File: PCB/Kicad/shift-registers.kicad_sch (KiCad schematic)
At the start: 7 parts

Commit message: routing
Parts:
- renumbered UVU-LINE3 to UVU-LINE1, UVU-LINE1 to UVU-LINE3
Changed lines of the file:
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@@
-(kicad_sch (version 20210126) (generator eeschema)
+(kicad_sch (version 20210406) (generator eeschema)
   (paper "A4")
   (no_connect (at 109.22 113.03))
@@
   (symbol (lib_id "power:+5V") (at 52.07 34.29 0) (unit 1)
     (in_bom yes) (on_board yes)
-    (property "Reference" "#PWR0151" (id 0) (at 52.07 38.1 0)
+    (property "Reference" "#PWR0141" (id 0) (at 52.07 38.1 0)
       (effects (font (size 1.27 1.27)) hide)
     )
@@
   (symbol (lib_id "power:+5V") (at 98.425 34.925 0) (unit 1)
     (in_bom yes) (on_board yes)
-    (property "Reference" "#PWR0150" (id 0) (at 98.425 38.735 0)
+    (property "Reference" "#PWR0142" (id 0) (at 98.425 38.735 0)
       (effects (font (size 1.27 1.27)) hide)
     )
@@
   (symbol (lib_id "power:+5V") (at 99.06 107.95 0) (unit 1)
     (in_bom yes) (on_board yes)
-    (property "Reference" "#PWR0135" (id 0) (at 99.06 111.76 0)
+    (property "Reference" "#PWR0146" (id 0) (at 99.06 111.76 0)
       (effects (font (size 1.27 1.27)) hide)
     )
@@
   (symbol (lib_id "power:+5V") (at 143.51 34.925 0) (unit 1)
     (in_bom yes) (on_board yes)
-    (property "Reference" "#PWR0149" (id 0) (at 143.51 38.735 0)
+    (property "Reference" "#PWR0143" (id 0) (at 143.51 38.735 0)
       (effects (font (size 1.27 1.27)) hide)
     )
@@
   (symbol (lib_id "power:+5V") (at 162.56 107.95 0) (unit 1)
     (in_bom yes) (on_board yes)
-    (property "Reference" "#PWR0152" (id 0) (at 162.56 111.76 0)
+    (property "Reference" "#PWR0147" (id 0) (at 162.56 111.76 0)
       (effects (font (size 1.27 1.27)) hide)
     )
@@
   (symbol (lib_id "power:+5V") (at 189.865 34.925 0) (unit 1)
     (in_bom yes) (on_board yes)
-    (property "Reference" "#PWR0148" (id 0) (at 189.865 38.735 0)
+    (property "Reference" "#PWR0144" (id 0) (at 189.865 38.735 0)
       (effects (font (size 1.27 1.27)) hide)
     )
@@
   (symbol (lib_id "power:+5V") (at 233.045 36.195 0) (unit 1)
     (in_bom yes) (on_board yes)
-    (property "Reference" "#PWR0147" (id 0) (at 233.045 40.005 0)
+    (property "Reference" "#PWR0145" (id 0) (at 233.045 40.005 0)
       (effects (font (size 1.27 1.27)) hide)
     )
@@
   (symbol (lib_id "74xx:74HC595") (at 143.51 50.165 0) (unit 1)
     (in_bom yes) (on_board yes)
-    (property "Reference" "UVU-LINE3" (id 0) (at 143.51 27.305 0))
+    (property "Reference" "UVU-LINE1" (id 0) (at 143.51 27.305 0))
     (property "Value" "74HC595" (id 1) (at 142.24 57.785 0))
     (property "Footprint" "Library:SO-16_3.9x9.9mm_P1.27mm" (id 2) (at 143.51 50.165 0)
@@
   (symbol (lib_id "74xx:74HC595") (at 233.045 51.435 0) (unit 1)
     (in_bom yes) (on_board yes)
-    (property "Reference" "UVU-LINE1" (id 0) (at 233.045 28.575 0))
+    (property "Reference" "UVU-LINE3" (id 0) (at 233.045 28.575 0))
     (property "Value" "74HC595" (id 1) (at 231.775 59.055 0))
     (property "Footprint" "Library:SO-16_3.9x9.9mm_P1.27mm" (id 2) (at 233.045 51.435 0)

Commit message: more routing
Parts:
- renumbered UVU-LINE3 to UVU-LINE1, UVU-LINE1 to UVU-LINE3
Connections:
- no-connect marks 4 -> 5
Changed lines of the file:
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@@
   (no_connect (at 109.22 130.81))
   (no_connect (at 172.72 113.03))
+  (no_connect (at 172.72 135.89))
   (no_connect (at 243.205 64.135))
   (wire (pts (xy 62.23 62.23) (xy 76.2 62.23))
@@
   (symbol (lib_id "74xx:74HC595") (at 143.51 50.165 0) (unit 1)
     (in_bom yes) (on_board yes)
-    (property "Reference" "UVU-LINE1" (id 0) (at 143.51 27.305 0))
+    (property "Reference" "UVU-LINE3" (id 0) (at 143.51 27.305 0))
     (property "Value" "74HC595" (id 1) (at 142.24 57.785 0))
     (property "Footprint" "Library:SO-16_3.9x9.9mm_P1.27mm" (id 2) (at 143.51 50.165 0)
@@
   (symbol (lib_id "74xx:74HC595") (at 233.045 51.435 0) (unit 1)
     (in_bom yes) (on_board yes)
-    (property "Reference" "UVU-LINE3" (id 0) (at 233.045 28.575 0))
+    (property "Reference" "UVU-LINE1" (id 0) (at 233.045 28.575 0))
     (property "Value" "74HC595" (id 1) (at 231.775 59.055 0))
     (property "Footprint" "Library:SO-16_3.9x9.9mm_P1.27mm" (id 2) (at 233.045 51.435 0)

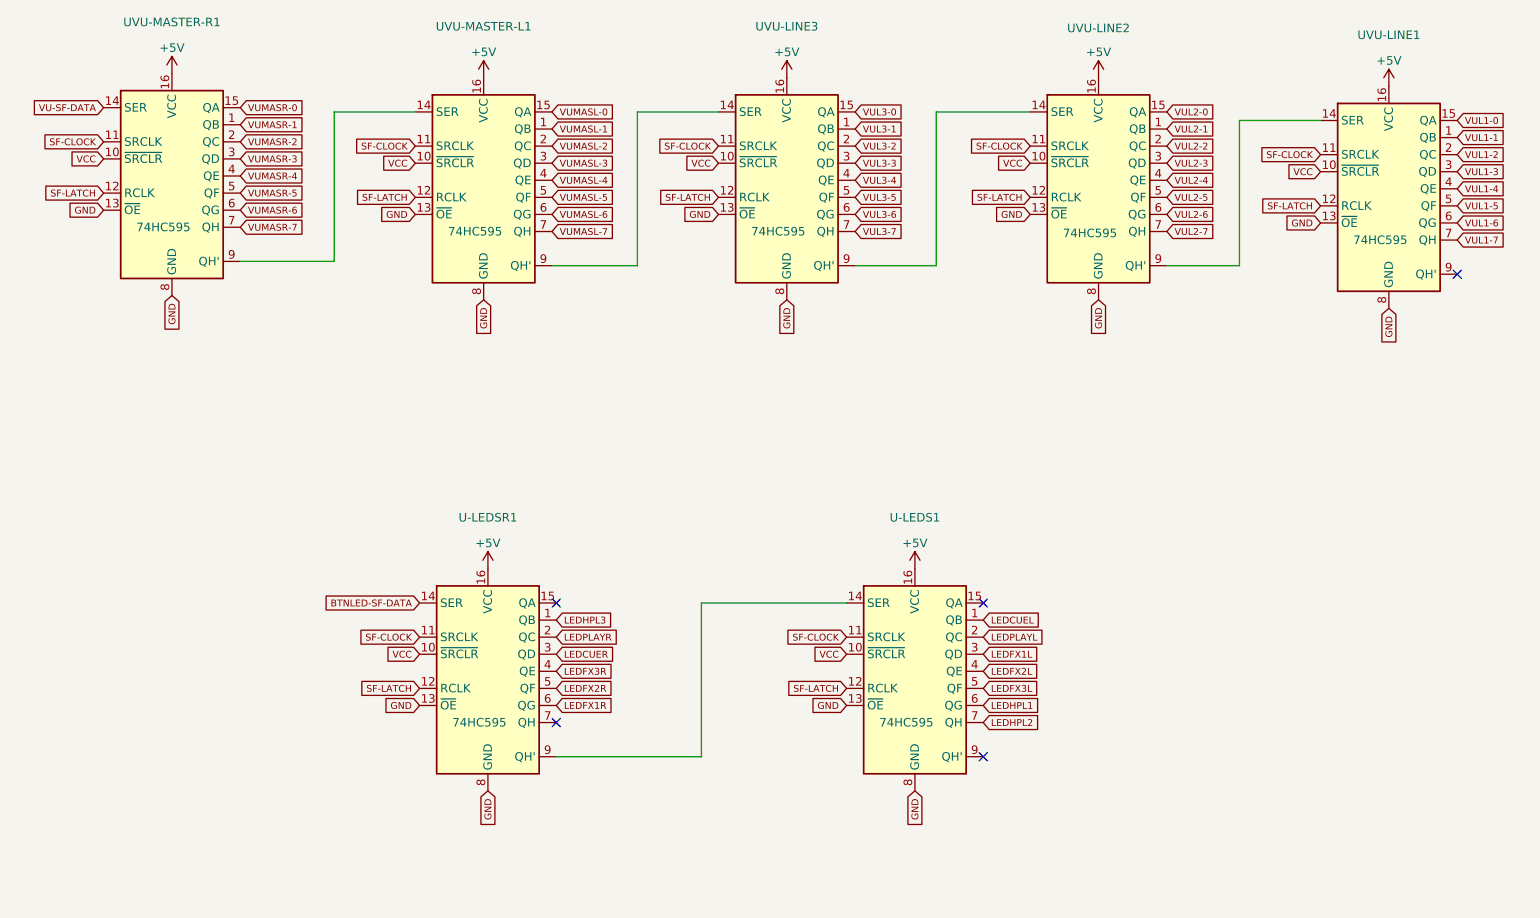
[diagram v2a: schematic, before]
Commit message: mistake fixed
added another latch pin for feedback leds SReg.
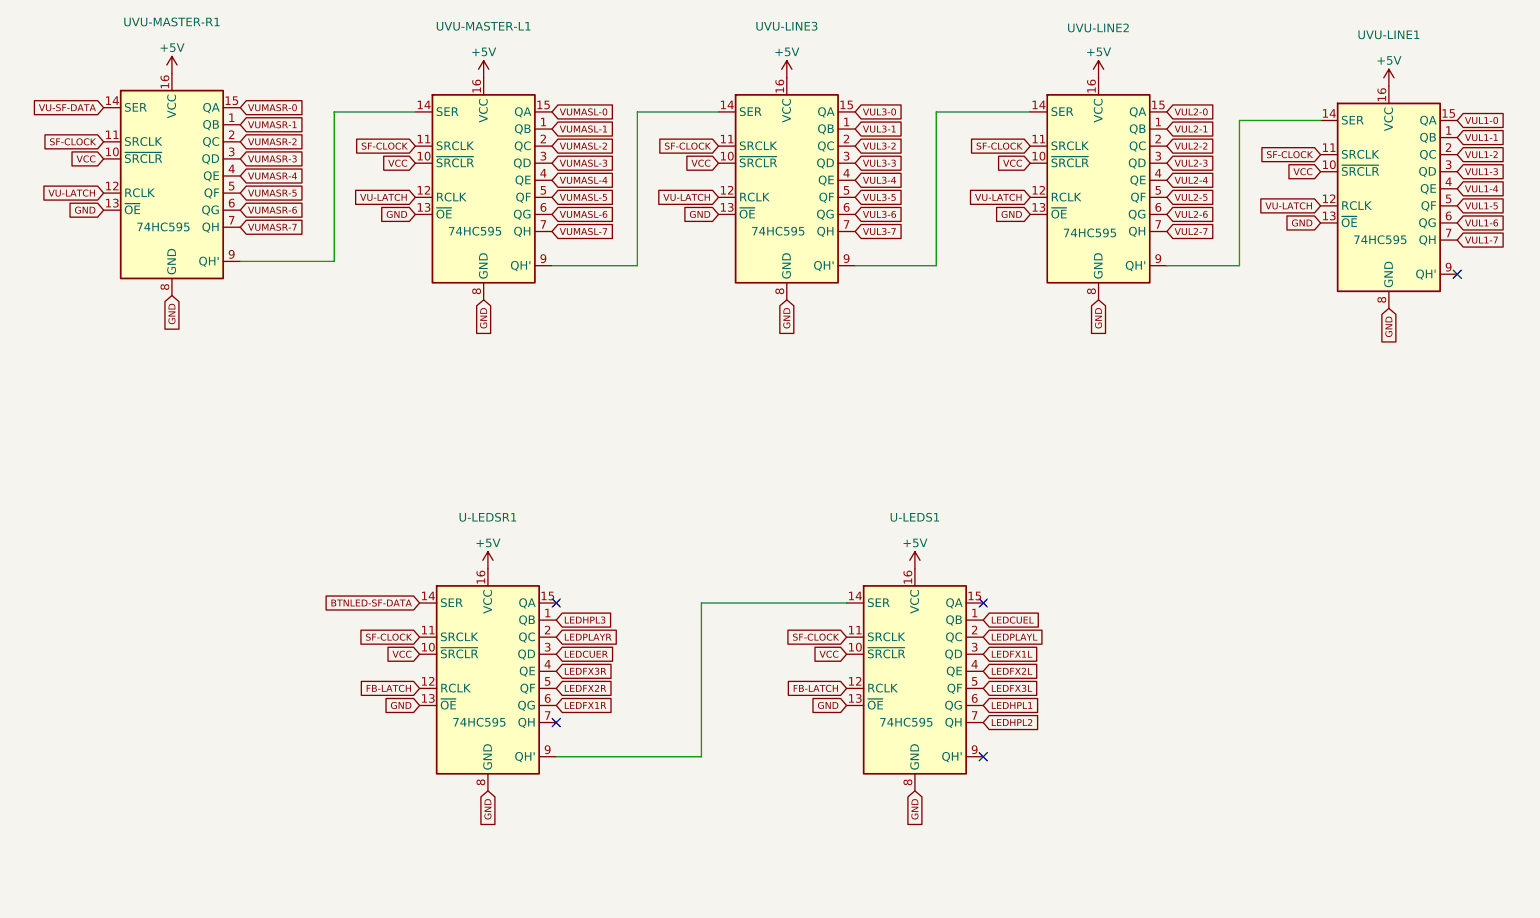
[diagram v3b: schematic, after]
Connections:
- net SF-LATCH renamed VU-LATCH
- net VU-LATCH: no longer U-LEDS1.12 (RCLK), U-LEDSR1.12 (RCLK)
- new net FB-LATCH: U-LEDS1.12 (RCLK), U-LEDSR1.12 (RCLK)
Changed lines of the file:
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@@
     )
   )
-  (global_label "SF-LATCH" (shape input) (at 41.91 52.07 180)
+  (global_label "VU-LATCH" (shape input) (at 41.91 52.07 180)
     (effects (font (size 1.016 1.016)) (justify right))
     (property "Intersheet References" "${INTERSHEET_REFS}" (id 0) (at 32.3354 52.0065 0)
@@
     )
   )
-  (global_label "SF-LATCH" (shape input) (at 88.265 52.705 180)
+  (global_label "VU-LATCH" (shape input) (at 88.265 52.705 180)
     (effects (font (size 1.016 1.016)) (justify right))
     (property "Intersheet References" "${INTERSHEET_REFS}" (id 0) (at 78.6904 52.6415 0)
@@
     )
   )
-  (global_label "SF-LATCH" (shape input) (at 88.9 125.73 180)
+  (global_label "FB-LATCH" (shape input) (at 88.9 125.73 180)
     (effects (font (size 1.016 1.016)) (justify right))
     (property "Intersheet References" "${INTERSHEET_REFS}" (id 0) (at 79.3254 125.6665 0)
@@
     )
   )
-  (global_label "SF-LATCH" (shape input) (at 133.35 52.705 180)
+  (global_label "VU-LATCH" (shape input) (at 133.35 52.705 180)
     (effects (font (size 1.016 1.016)) (justify right))
     (property "Intersheet References" "${INTERSHEET_REFS}" (id 0) (at 123.7754 52.6415 0)
@@
     )
   )
-  (global_label "SF-LATCH" (shape input) (at 152.4 125.73 180)
+  (global_label "FB-LATCH" (shape input) (at 152.4 125.73 180)
     (effects (font (size 1.016 1.016)) (justify right))
     (property "Intersheet References" "${INTERSHEET_REFS}" (id 0) (at 142.8254 125.6665 0)
@@
     )
   )
-  (global_label "SF-LATCH" (shape input) (at 179.705 52.705 180)
+  (global_label "VU-LATCH" (shape input) (at 179.705 52.705 180)
     (effects (font (size 1.016 1.016)) (justify right))
     (property "Intersheet References" "${INTERSHEET_REFS}" (id 0) (at 170.1304 52.6415 0)
@@
     )
   )
-  (global_label "SF-LATCH" (shape input) (at 222.885 53.975 180)
+  (global_label "VU-LATCH" (shape input) (at 222.885 53.975 180)
     (effects (font (size 1.016 1.016)) (justify right))
     (property "Intersheet References" "${INTERSHEET_REFS}" (id 0) (at 213.3104 53.9115 0)

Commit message: schematic updated
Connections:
- net LEDLOOPL: now reaches U-LEDS1.15 (QA)
- net LEDLOOPR: now reaches U-LEDSR1.15 (QA)
- no-connect marks 5 -> 3
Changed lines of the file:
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@@
 (kicad_sch (version 20210406) (generator eeschema)
   (paper "A4")
-  (no_connect (at 109.22 113.03))
   (no_connect (at 109.22 130.81))
-  (no_connect (at 172.72 113.03))
   (no_connect (at 172.72 135.89))
   (no_connect (at 243.205 64.135))
@@
     )
   )
+  (global_label "LEDLOOPR" (shape input) (at 109.22 113.03 0)
+    (effects (font (size 1.016 1.016)) (justify left))
+    (property "Intersheet References" "${INTERSHEET_REFS}" (id 0) (at 43.688 202.438 0)
+      (effects (font (size 1.016 1.016)) hide)
+    )
+  )
   (global_label "LEDHPL3" (shape input) (at 109.22 115.57 0)
     (effects (font (size 1.016 1.016)) (justify left))
@@
     )
   )
+  (global_label "LEDLOOPL" (shape input) (at 172.72 113.03 0)
+    (effects (font (size 1.016 1.016)) (justify left))
+    (property "Intersheet References" "${INTERSHEET_REFS}" (id 0) (at 107.188 199.898 0)
+      (effects (font (size 1.016 1.016)) hide)
+    )
+  )

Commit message: tracking WIP
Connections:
- net LEDCUEL: now also U-LEDS1.4 (QE); no longer U-LEDS1.1 (QB)
- net LEDCUER: now also U-LEDSR1.2 (QC); no longer U-LEDSR1.3 (QD)
- net LEDFX1L: now also U-LEDS1.2 (QC); no longer U-LEDS1.3 (QD)
- net LEDFX2L: now also U-LEDS1.1 (QB); no longer U-LEDS1.4 (QE)
- net LEDFX3L: now also U-LEDS1.15 (QA); no longer U-LEDS1.5 (QF)
- net LEDHPL3: now also U-LEDSR1.15 (QA); no longer U-LEDSR1.1 (QB)
- net LEDLOOPL: now also U-LEDS1.5 (QF); no longer U-LEDS1.15 (QA)
- net LEDLOOPR: now also U-LEDSR1.3 (QD); no longer U-LEDSR1.15 (QA)
- net LEDPLAYL: now also U-LEDS1.3 (QD); no longer U-LEDS1.2 (QC)
- net LEDPLAYR: now also U-LEDSR1.1 (QB); no longer U-LEDSR1.2 (QC)
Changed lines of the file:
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@@
     )
   )
-  (global_label "LEDLOOPR" (shape input) (at 109.22 113.03 0)
+  (global_label "LEDHPL3" (shape input) (at 109.22 113.03 0)
     (effects (font (size 1.016 1.016)) (justify left))
-    (property "Intersheet References" "${INTERSHEET_REFS}" (id 0) (at 43.688 202.438 0)
-      (effects (font (size 1.016 1.016)) hide)
-    )
-  )
-  (global_label "LEDHPL3" (shape input) (at 109.22 115.57 0)
-    (effects (font (size 1.016 1.016)) (justify left))
-    (property "Intersheet References" "${INTERSHEET_REFS}" (id 0) (at 43.688 26.162 0)
+    (property "Intersheet References" "${INTERSHEET_REFS}" (id 0) (at 43.688 23.622 0)
       (effects (font (size 1.27 1.27)) hide)
     )
   )
-  (global_label "LEDPLAYR" (shape input) (at 109.22 118.11 0)
+  (global_label "LEDPLAYR" (shape input) (at 109.22 115.57 0)
     (effects (font (size 1.016 1.016)) (justify left))
-    (property "Intersheet References" "${INTERSHEET_REFS}" (id 0) (at 43.688 217.678 0)
+    (property "Intersheet References" "${INTERSHEET_REFS}" (id 0) (at 43.688 215.138 0)
       (effects (font (size 1.27 1.27)) hide)
     )
   )
-  (global_label "LEDCUER" (shape input) (at 109.22 120.65 0)
+  (global_label "LEDCUER" (shape input) (at 109.22 118.11 0)
     (effects (font (size 1.016 1.016)) (justify left))
-    (property "Intersheet References" "${INTERSHEET_REFS}" (id 0) (at 43.688 217.678 0)
+    (property "Intersheet References" "${INTERSHEET_REFS}" (id 0) (at 43.688 215.138 0)
       (effects (font (size 1.27 1.27)) hide)
+    )
+  )
+  (global_label "LEDLOOPR" (shape input) (at 109.22 120.65 0)
+    (effects (font (size 1.016 1.016)) (justify left))
+    (property "Intersheet References" "${INTERSHEET_REFS}" (id 0) (at 43.688 210.058 0)
+      (effects (font (size 1.016 1.016)) hide)
     )
   )
   (global_label "LEDFX3R" (shape input) (at 109.22 123.19 0)
     (effects (font (size 1.016 1.016)) (justify left))
-    (property "Intersheet References" "${INTERSHEET_REFS}" (id 0) (at 117.7302 123.2535 0)
+    (property "Intersheet References" "${INTERSHEET_REFS}" (id 0) (at 117.7302 123.1265 0)
       (effects (font (size 1.016 1.016)) (justify left) hide)
     )
@@
     )
   )
-  (global_label "LEDLOOPL" (shape input) (at 172.72 113.03 0)
+  (global_label "LEDFX3L" (shape input) (at 172.72 113.03 0)
     (effects (font (size 1.016 1.016)) (justify left))
-    (property "Intersheet References" "${INTERSHEET_REFS}" (id 0) (at 107.188 199.898 0)
+    (property "Intersheet References" "${INTERSHEET_REFS}" (id 0) (at 181.0367 112.9665 0)
+      (effects (font (size 1.016 1.016)) (justify left) hide)
+    )
+  )
+  (global_label "LEDFX2L" (shape input) (at 172.72 115.57 0)
+    (effects (font (size 1.016 1.016)) (justify left))
+    (property "Intersheet References" "${INTERSHEET_REFS}" (id 0) (at 181.0367 115.6335 0)
+      (effects (font (size 1.016 1.016)) (justify left) hide)
+    )
+  )
+  (global_label "LEDFX1L" (shape input) (at 172.72 118.11 0)
+    (effects (font (size 1.016 1.016)) (justify left))
+    (property "Intersheet References" "${INTERSHEET_REFS}" (id 0) (at 181.0367 118.1735 0)
+      (effects (font (size 1.016 1.016)) (justify left) hide)
+    )
+  )
+  (global_label "LEDPLAYL" (shape input) (at 172.72 120.65 0)
+    (effects (font (size 1.016 1.016)) (justify left))
+    (property "Intersheet References" "${INTERSHEET_REFS}" (id 0) (at 107.188 215.138 0)
+      (effects (font (size 1.27 1.27)) hide)
+    )
+  )
+  (global_label "LEDCUEL" (shape input) (at 172.72 123.19 0)
+    (effects (font (size 1.016 1.016)) (justify left))
+    (property "Intersheet References" "${INTERSHEET_REFS}" (id 0) (at 107.188 215.138 0)
+      (effects (font (size 1.27 1.27)) hide)
+    )
+  )
+  (global_label "LEDLOOPL" (shape input) (at 172.72 125.73 0)
+    (effects (font (size 1.016 1.016)) (justify left))
+    (property "Intersheet References" "${INTERSHEET_REFS}" (id 0) (at 107.188 212.598 0)
       (effects (font (size 1.016 1.016)) hide)
     )
   )
-  (global_label "LEDCUEL" (shape input) (at 172.72 115.57 0)
-    (effects (font (size 1.016 1.016)) (justify left))
-    (property "Intersheet References" "${INTERSHEET_REFS}" (id 0) (at 107.188 23.622 0)
-      (effects (font (size 1.27 1.27)) hide)
-    )
-  )
-  (global_label "LEDPLAYL" (shape input) (at 172.72 118.11 0)
-    (effects (font (size 1.016 1.016)) (justify left))
-    (property "Intersheet References" "${INTERSHEET_REFS}" (id 0) (at 107.188 23.622 0)
-      (effects (font (size 1.27 1.27)) hide)
-    )
-  )
-  (global_label "LEDFX1L" (shape input) (at 172.72 120.65 0)
-    (effects (font (size 1.016 1.016)) (justify left))
-    (property "Intersheet References" "${INTERSHEET_REFS}" (id 0) (at 181.0367 120.5865 0)
-      (effects (font (size 1.016 1.016)) (justify left) hide)
-    )
-  )
-  (global_label "LEDFX2L" (shape input) (at 172.72 123.19 0)
-    (effects (font (size 1.016 1.016)) (justify left))
-    (property "Intersheet References" "${INTERSHEET_REFS}" (id 0) (at 181.0367 123.1265 0)
-      (effects (font (size 1.016 1.016)) (justify left) hide)
-    )
-  )
-  (global_label "LEDFX3L" (shape input) (at 172.72 125.73 0)
-    (effects (font (size 1.016 1.016)) (justify left))
-    (property "Intersheet References" "${INTERSHEET_REFS}" (id 0) (at 181.0367 125.6665 0)
-      (effects (font (size 1.016 1.016)) (justify left) hide)
-    )
-  )
